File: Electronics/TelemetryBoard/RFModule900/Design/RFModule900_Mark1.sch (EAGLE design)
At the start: 166 parts, among them T1 DC08-73, T2 DC08-73, U1 TPS2561, U2 TPS2561, U3 LM75B, U4 LTC5505, U5 LTC5505, U6 MCP4728, U7 ADC128D818, U8 MIC5504-3.3YM5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

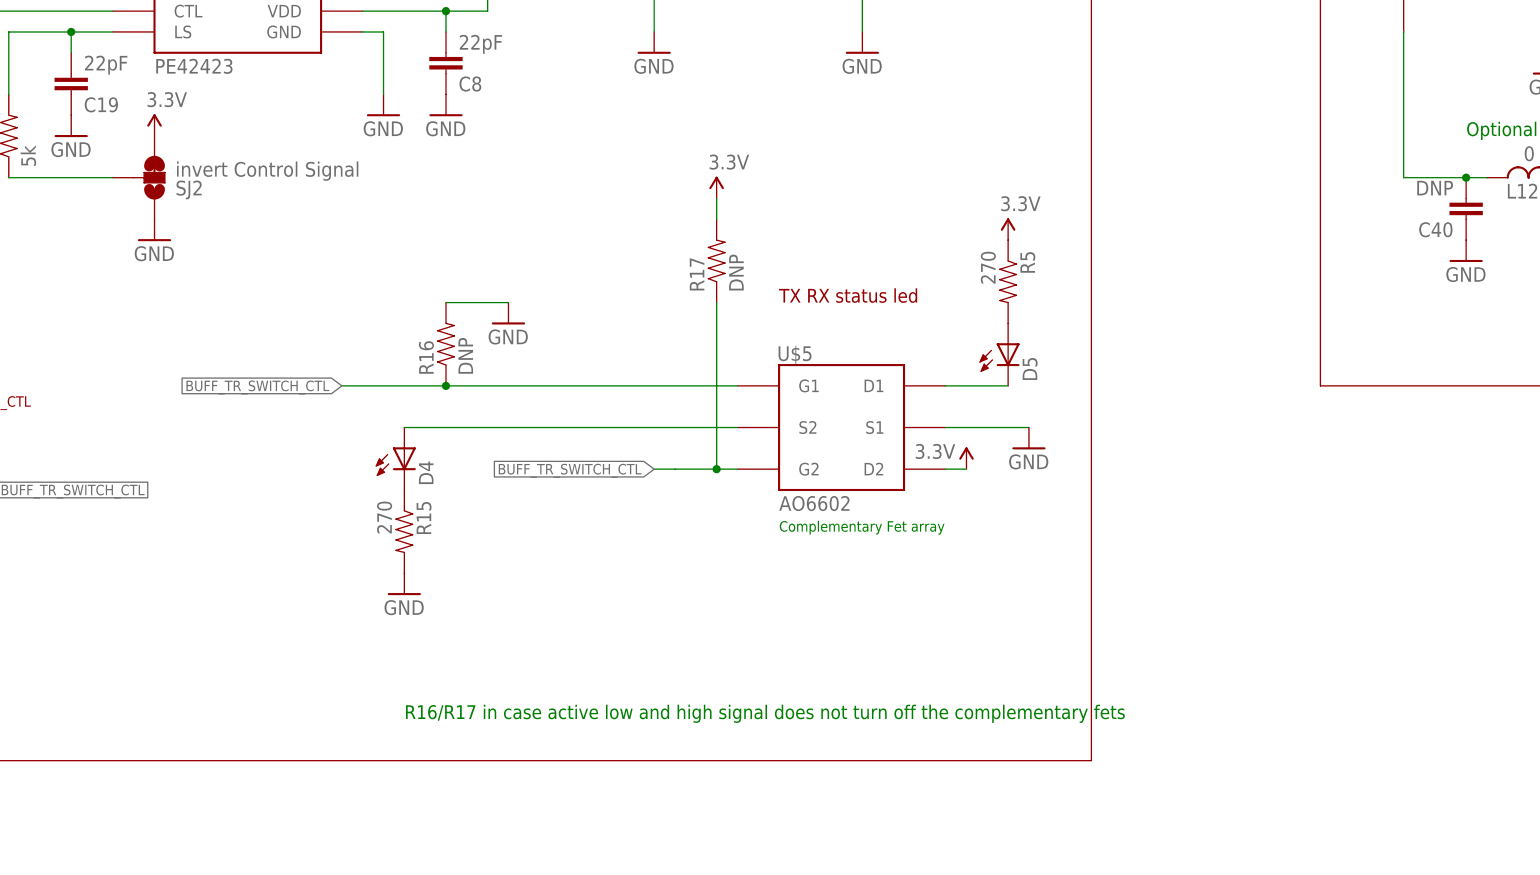
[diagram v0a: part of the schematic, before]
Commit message: Simplified RX TX led driving
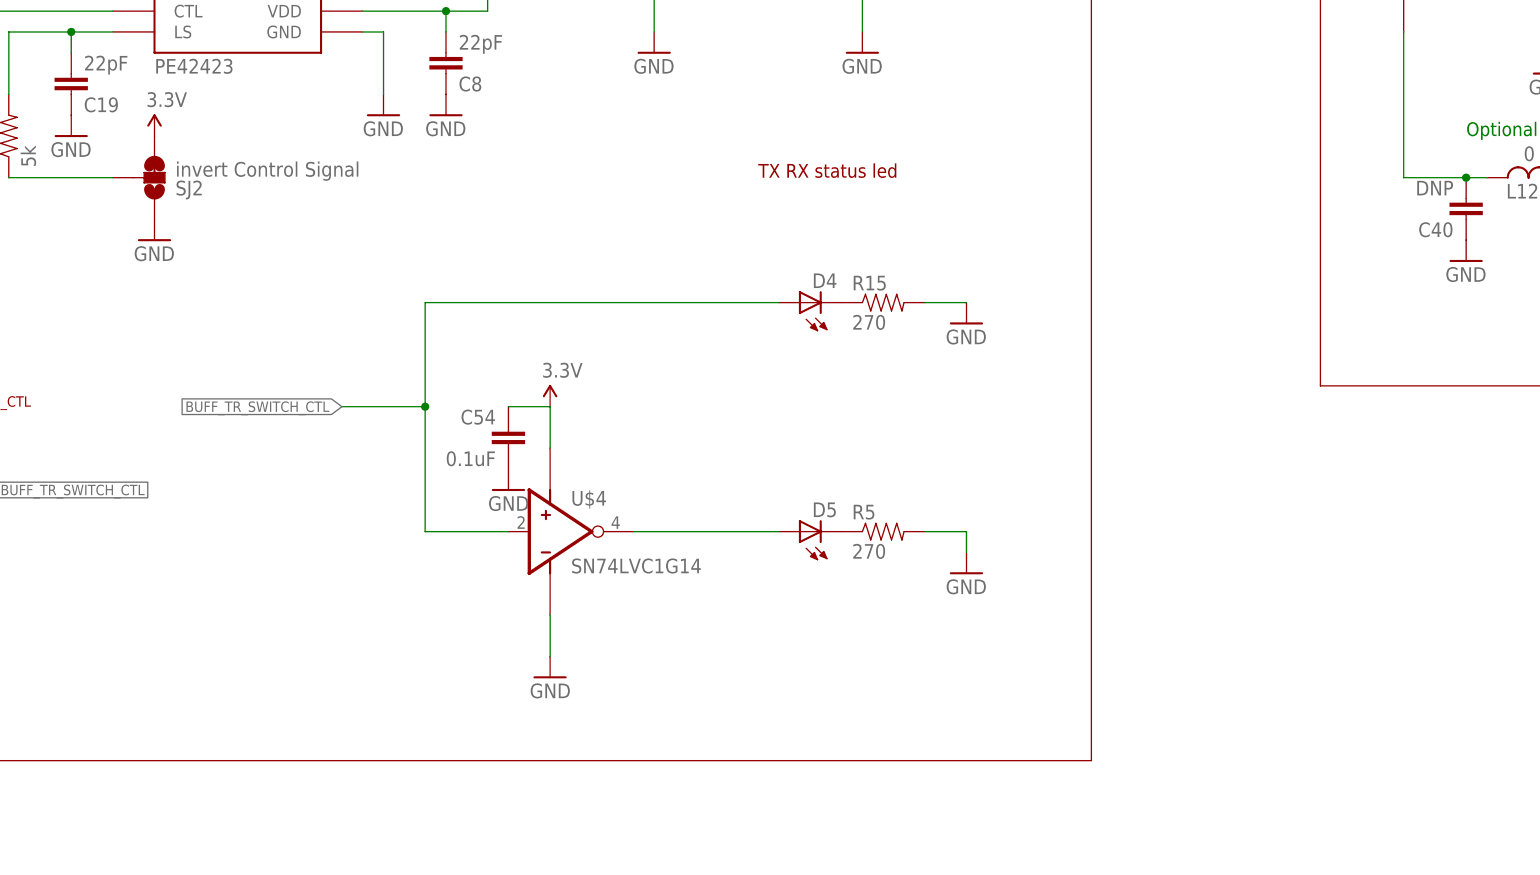
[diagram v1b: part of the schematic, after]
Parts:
- removed R16, R17: DNP, SparkFun-Resistors:RESISTOR0402-RES
- removed U$5: AO6602, RitLaunchInitiative:AO6602
- added C54: 0.1uF, SparkFun-Capacitors:CAP0402-CAP
- added U$4: SN74LVC1G14, RitLaunchInitiative:SN74LVC1G14
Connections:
- removed net N$35: D4.A, U$5.S2
- removed net N$52: R17.1, U$5.G2
- net 3.3V: now also C54.1, U$4.VCC; no longer R17.2, R5.1, U$5.D2
- net BUFF_TR_SWITCH_CTL: now also D4.A, U$4.I; no longer R16.1, U$5.G1
- net GND: now also C54.2, R5.2, U$4.GND; no longer R16.2, U$5.S1
- net N$33: now also D5.C, R5.1; no longer D5.A, R5.2
- net N$34: now also D5.A, U$4.O; no longer D5.C, U$5.D1
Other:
- note removed: "Complementary Fet array"
- note removed: "R16/R17 in case active low and high signal does not turn off the complementary fets"
- moved on the sheet: D4, D5, R15, R5
